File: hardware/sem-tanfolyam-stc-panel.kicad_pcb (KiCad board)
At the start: 2 copper layers, 18 x 42.7 mm, 28 parts, among them J1 Conn_01x09_Male, J2 Conn_01x09_Male, J3 USB_C_Receptacle_USB2.0, Q1 MMBT3906, Q2 AO3401, SW1 SW_Push, U1 CH340E, U2 STC8G1K08

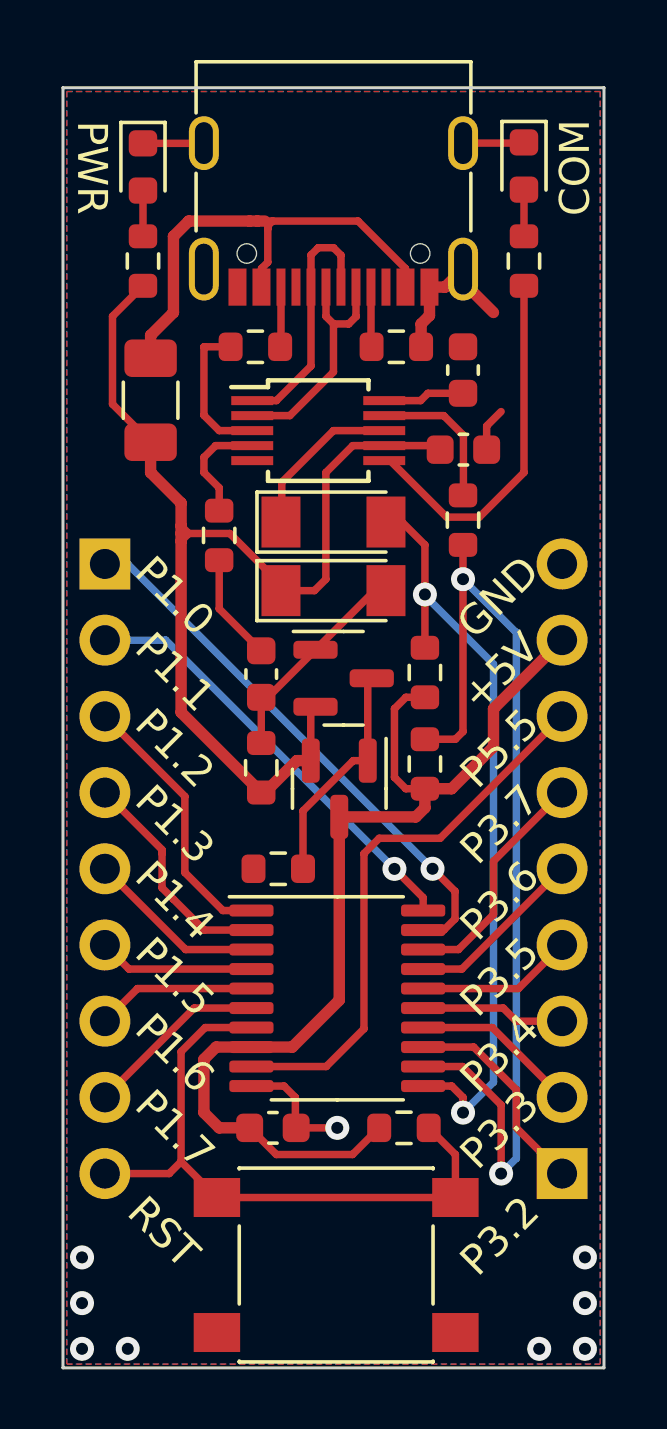
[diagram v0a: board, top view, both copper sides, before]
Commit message: BOM hozzáadva + hiányosságok meggyógyítva.
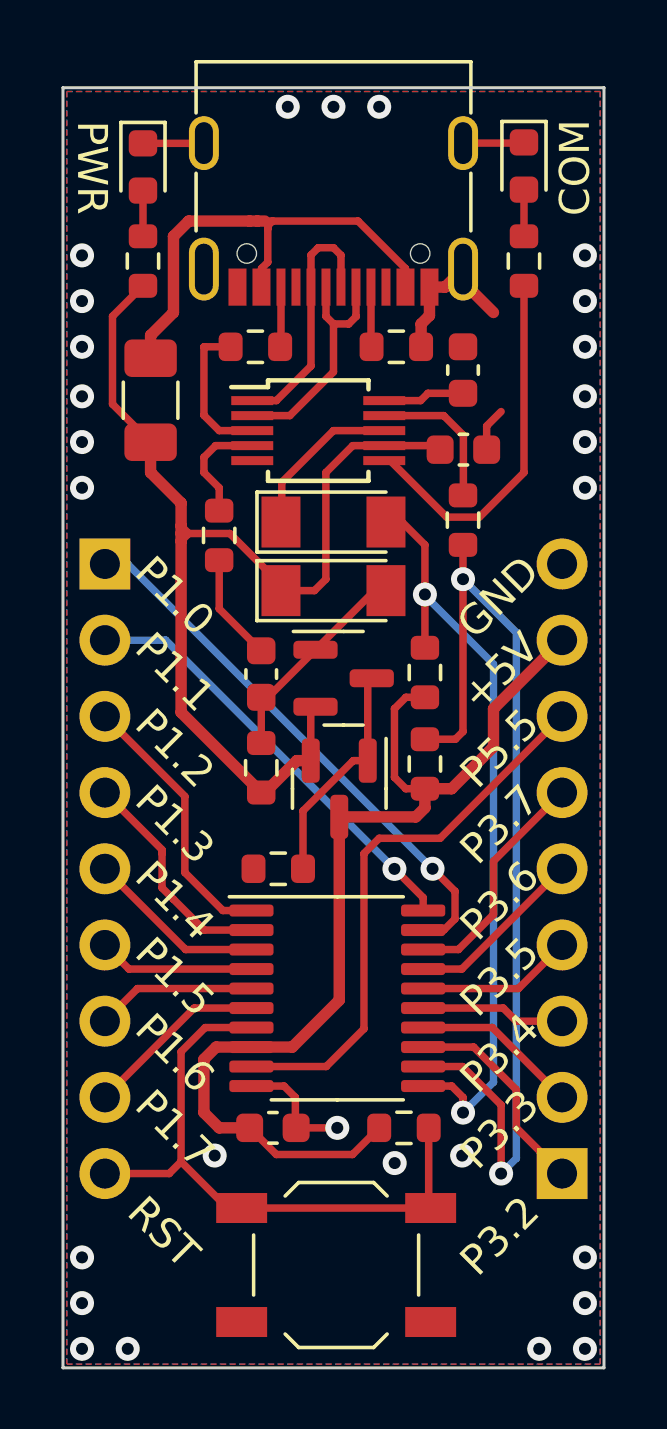
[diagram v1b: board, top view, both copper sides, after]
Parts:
- SW1: footprint Button_Switch_SMD:SW_Push_1P1T_NO_6x6mm_H9.5mm -> Button_Switch_SMD:SW_SPST_TL3342
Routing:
- net /RST: track 21.4 -> 20.6 mm
- net GND: vias 9 -> 27
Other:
- board text added: "Elkövető: W.P."
- board text added: "Rev.A"

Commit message: Összemontírozva, gyártásra készen.
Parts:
- J3: footprint Connector_USB:USB_C_Receptacle_G-Switch_GT-USB-7010ASV -> jlcpcb_rotation:USB_C_Receptacle_G-Switch_GT-USB-7010ASV
- Q1, Q2: footprint Package_TO_SOT_SMD:SOT-23 -> jlcpcb_rotation:SOT-23
- U1: footprint Package_SO:MSOP-10_3x3mm_P0.5mm -> jlcpcb_rotation:MSOP-10_3x3mm_P0.5mm
- U2: footprint Package_SO:TSSOP-20_4.4x6.5mm_P0.65mm -> jlcpcb_rotation:TSSOP-20_4.4x6.5mm_P0.65mm
- moved J3 1.30 mm to (124.5, 69.6)
- turned Q1 to 180 degrees
- turned Q2 to 90 degrees
- turned U1 to -90 degrees
- turned U2 to -90 degrees
